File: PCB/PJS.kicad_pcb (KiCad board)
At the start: 2 copper layers, 127 x 127 mm, 41 parts, among them J1 HFW8R-1STE1H1LF_FFC, J10 SM02B-PASS-TBT_SwitchConnector, J2 SM02B-PASS-TBT_Connector, J3 SM02B-PASS-TBT_Connector, J4 SM02B-PASS-TBT_Connector, J5 SM02B-PASS-TBT_Connector, J6 SM02B-PASS-TBT_SwitchConnector, J7 SM02B-PASS-TBT_SwitchConnector, J8 SM02B-PASS-TBT_SwitchConnector, J9 SM02B-PASS-TBT_SwitchConnector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

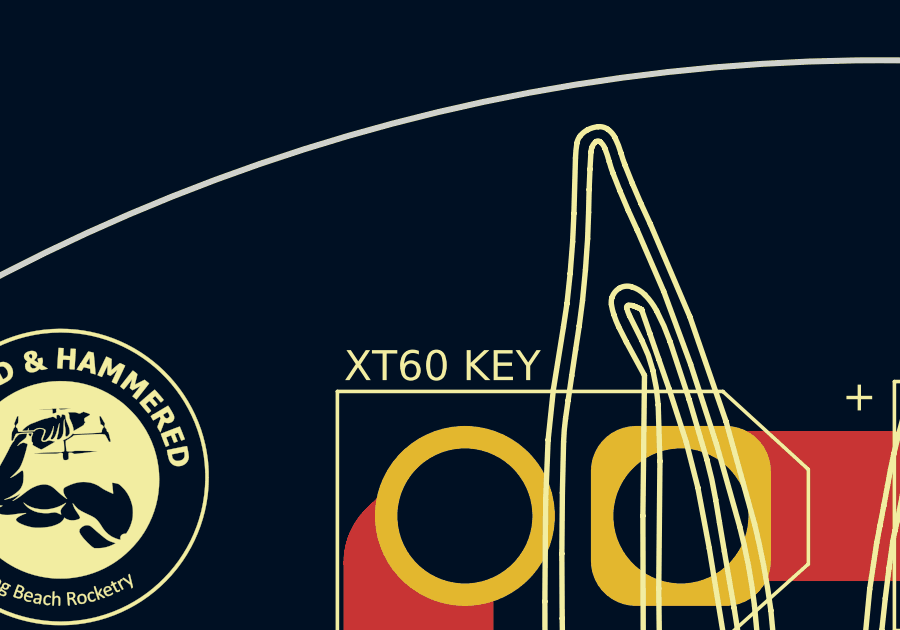
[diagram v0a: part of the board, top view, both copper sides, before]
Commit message: silkscreen adjustments
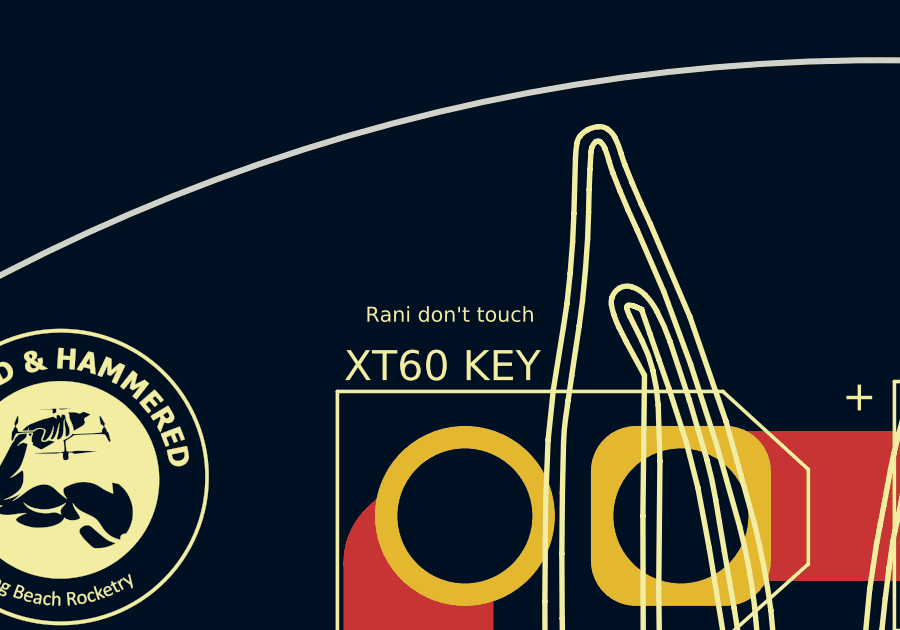
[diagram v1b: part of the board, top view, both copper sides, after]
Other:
- board text added: "Rani don't touch"

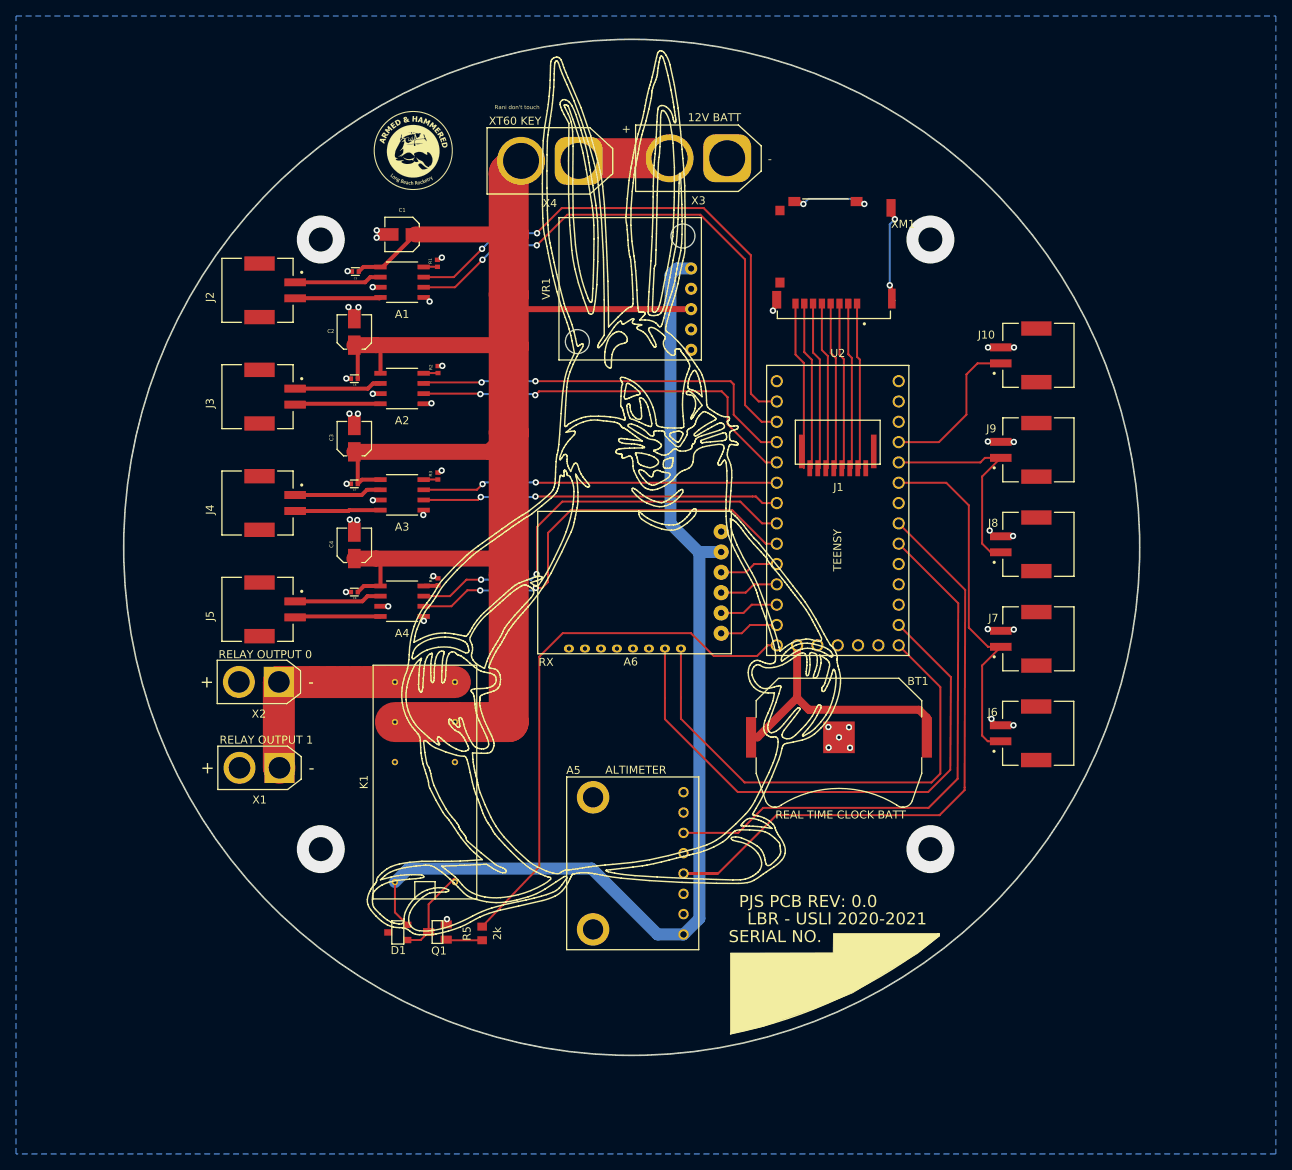
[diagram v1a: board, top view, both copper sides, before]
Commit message: Grounded DRV8871s, sizde traces, and general neatness
There are now vias to for the motor drivers to manage heat. Capacitors were moved slightly. Traces are now sized, and aligned.

There is huge overhead for each trace, with the exception of signal.

The two issues that still need to be addressed are the XT60s and the Relay, both of which are not going to the right pins.
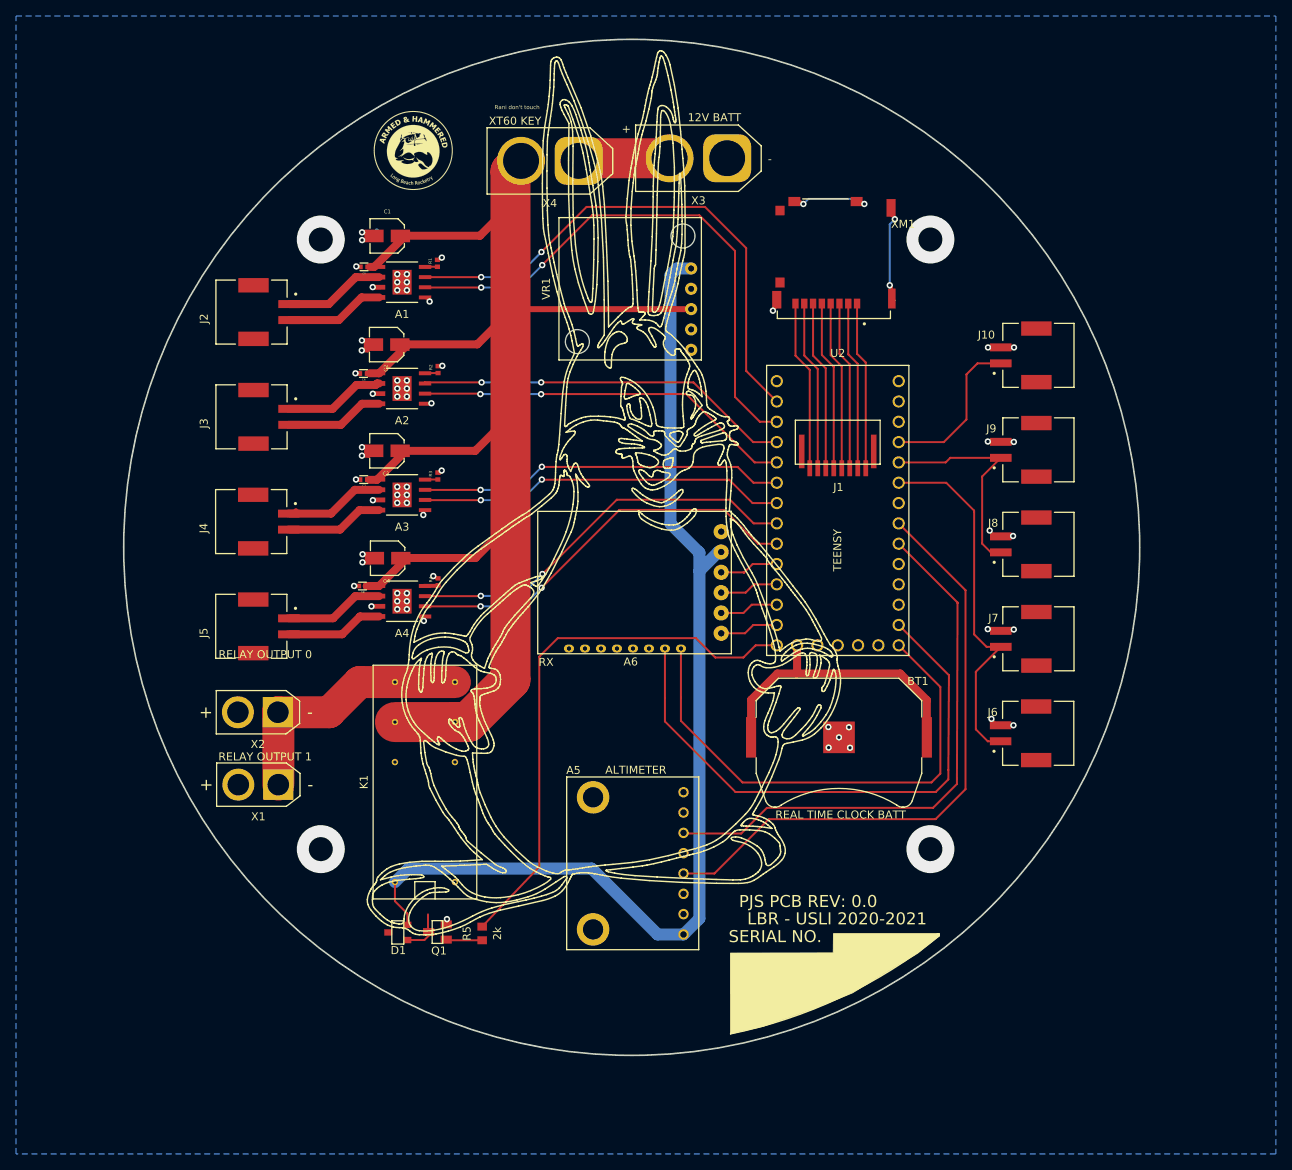
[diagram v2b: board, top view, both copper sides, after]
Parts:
- moved C4 4.46 mm to (100.4, 100.2), turned to 180 degrees
- moved C3 4.35 mm to (100.3, 86.7), turned to 180 degrees
- moved C2 4.34 mm to (100.3, 73.5), turned to 180 degrees
- moved X2 3.79 mm to (86.7, 119.4)
- moved J2 2.82 mm to (84.2, 69.4)
- moved J3 2.63 mm to (84.2, 82.5)
- moved J4 2.45 mm to (84.2, 95.6)
- moved J5 2.26 mm to (84.2, 108.7)
- moved X1 2.11 mm to (86.8, 128.5)
- moved C1 1.87 mm to (100.4, 59.9)
- moved C6 1.32 mm to (97.4, 77.1)
- moved C7 1.29 mm to (97.4, 90.3)
- moved C8 1.27 mm to (97.3, 103.6)
- moved C5 1.23 mm to (97.5, 63.7)
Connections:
- X4 pad 2: (no net) -> +12V
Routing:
- net +12V: track 211.5 -> 197.3 mm
- net /UAS_DriverOUT2: track 21.1 -> 12.4 mm
- net Net-(D1-Pad2): track 11.1 -> 5.58 mm
- net /Alt_SCK: track 80.4 -> 76.3 mm
- net /LockB_DriverIN2: track 54.5 -> 50.7 mm
- net /3.3V_Coin: track 34.1 -> 37.7 mm
- net /LockB_DriverIN1: track 53.6 -> 50.2 mm
- net /Link_DriverIN2: track 50.1 -> 47.8 mm
- net /Link_DriverIN1: track 49.6 -> 47.5 mm
- net /LockA_DriverOUT1: track 10.9 -> 12.7 mm
- net /UAS_DriverOUT1: track 10.9 -> 12.6 mm
- net /Link_DriverOUT2: track 10.7 -> 12.3 mm
- net /Link_DriverOUT1: track 10.9 -> 12.6 mm
- net /LockA_DriverIN2: track 44.7 -> 46.3 mm
- net /LockA_DriverOUT2: track 10.7 -> 12.3 mm
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
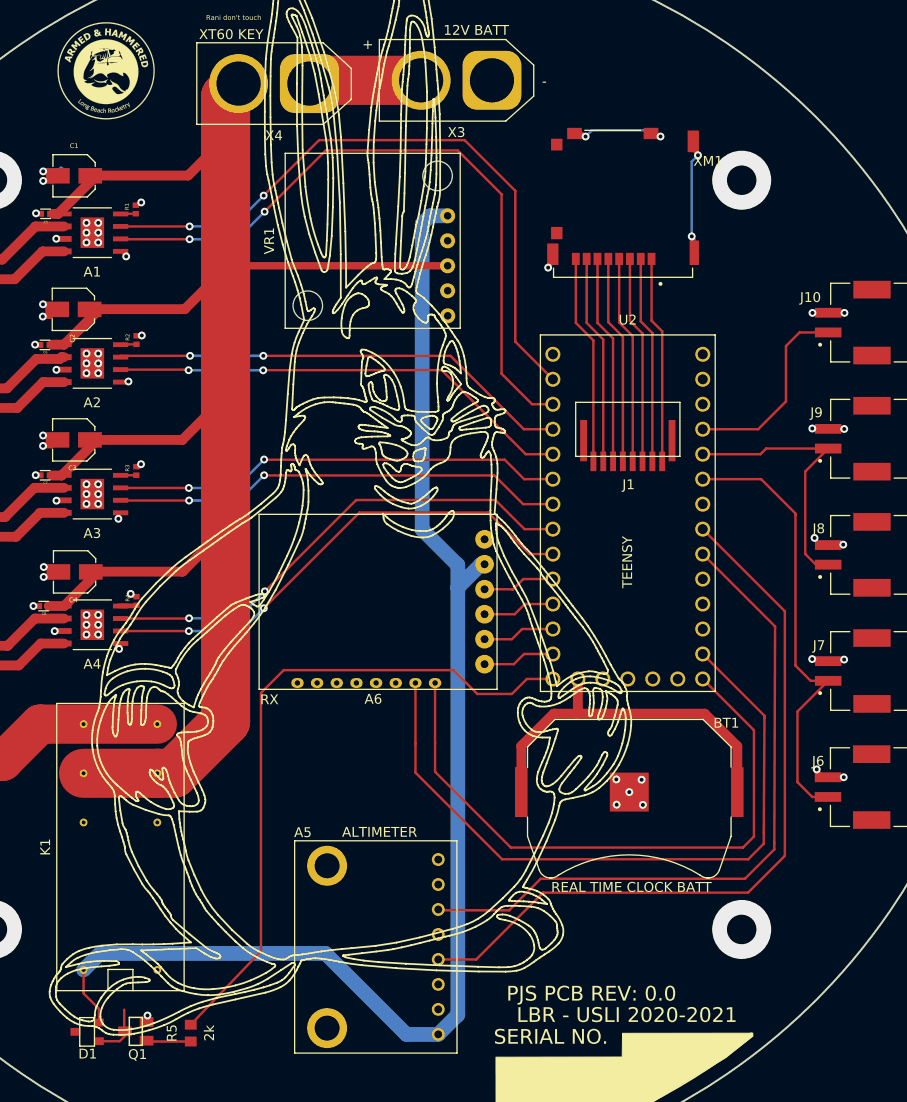
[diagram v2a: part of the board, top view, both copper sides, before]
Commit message: Finished PCB
All traces are sized and spaced. The XT60 and relay pins are fixed.
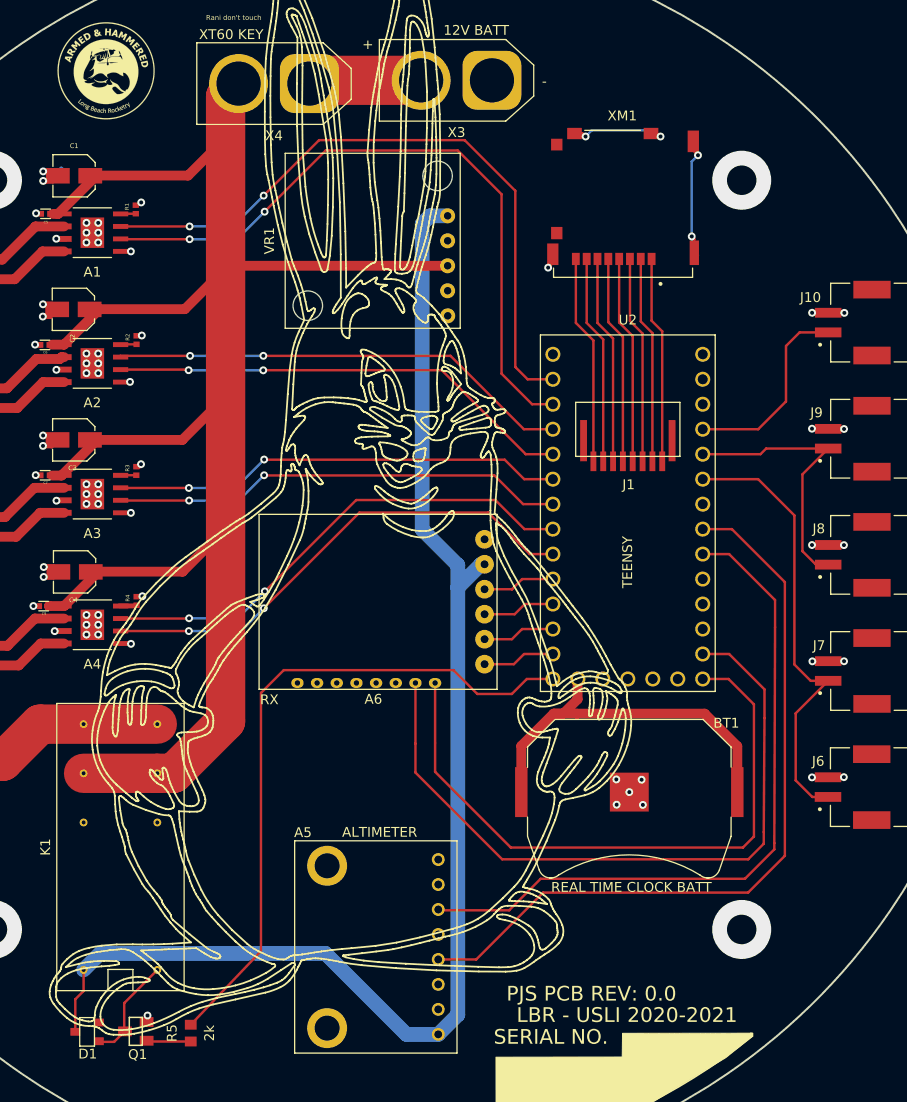
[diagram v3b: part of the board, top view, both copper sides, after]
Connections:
- D1 pad 1: +5V -> Net-(D1-Pad1)
- D1 pad 3: (no net) -> +5V
- K1 pad 8: Net-(D1-Pad2) -> Net-(D1-Pad1)
- Q1 pad 3: Net-(D1-Pad2) -> Net-(D1-Pad1)
- X3 pad 2: (no net) -> Net-(X3-Pad2)
- X4 pad 1: (no net) -> Net-(X3-Pad2)
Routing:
- net Net-(X3-Pad2): track 0.00 -> 11.5 mm
- net (no net): track 11.5 -> 0.00 mm
- net Net-(D1-Pad1): track 0.00 -> 10.8 mm
- net +12V: track 197.3 -> 189.4 mm
- net Net-(D1-Pad2): track 5.58 -> 0.00 mm
- net GND: track 72.4 -> 76.1 mm
- net /Alt_SCK: track 76.3 -> 78.0 mm
- net /3.3V_Coin: track 37.7 -> 39.4 mm
- net /RF_CH6: track 70.7 -> 72.3 mm
- net /Alt_SDI: track 69.9 -> 71.4 mm
- net /RF_CH5: track 63.6 -> 65.1 mm
- net /UAS_DriverIN1: track 66.7 -> 68.2 mm
- net +5V: track 137.6 -> 138.2 mm
